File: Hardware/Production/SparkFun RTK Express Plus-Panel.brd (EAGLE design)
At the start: 219.3 x 141.9 mm, 507 parts, among them J13 Internal, J16 MICRO-SD-PUSH-PUSH-EXT-PIN, J17 Qwiic Right Angle, J19 External, J21 USB Female Type C Connector, J24 USB Female Type C Connector, J3 USB Female Type C Connector, J31 Qwiic Right Angle, J32 Internal, J38 MICRO-SD-PUSH-PUSH-EXT-PIN, J39 External, J4 External, J40 USB Female Type C Connector, J43 USB Female Type C Connector, J5 USB Female Type C Connector, J50 Qwiic Right Angle, J51 Internal, J57 MICRO-SD-PUSH-PUSH-EXT-PIN, Q1 SIL2308-TP, Q2 MBT3904DW1T1, Q3 MBT3904DW1T1, Q4 SIL2308-TP, Q5 MBT3904DW1T1, Q6 SIL2308-TP, U1 74HC4052D, U10 MCP73833, U11 U-BLOX_ZED_F9R, U12 CH340C, U13 LIS2DH12, U14 MAX17048, U15 STLQ015-3.3V, U16 MCP73833, U17 74HC4052D, U18 LIS2DH12, U19 ESP-WROOM-3232D-NARROW, U2 AP2112K-3.3, U20 NC7SZ14-D, U21 NC7SZ14-D, U22 U-BLOX_ZED_F9R, U23 AP2112K-3.3, U24 CH340C, U25 MAX17048, U26 STLQ015-3.3V, U27 MCP73833, U28 74HC4052D, U29 LIS2DH12, U3 AP2112K-3.3, U30 ESP-WROOM-3232D-NARROW, U31 NC7SZ14-D, U32 NC7SZ14-D, U33 U-BLOX_ZED_F9R, U4 STLQ015-3.3V, U5 ESP-WROOM-3232D-NARROW, U6 CH340C, U7 MAX17048, U8 NC7SZ14-D, U9 NC7SZ14-D

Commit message: Create panel files for v11 PCB
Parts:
- added R88, R92, R93: 10k, SparkFun-Resistors:0603
- added R89: 3.3k, SparkFun-Resistors:0603
- added R90, R91: 33, SparkFun-Resistors:1206_RA
- R10: value 10 -> 27
- R11: value 100k -> 27
- R12: value 5.1k -> 10
- R21, R70: value 5.1k -> 100k
- R32: value 1k -> 5.1k
- R35, R42: value 100k -> 5.1k
- R36: value 10k -> 1k
- R39, R55, R75, R84: value 10k -> 100k
- R40, R41: value 5.1k -> 10k
- R43: value 470 -> 5.1k
- R44: value 150k -> 100k
- R45: value 0 -> 470
- R46: value 10k -> 150k
- R47: value 1k -> 0
- R48, R57, R79, R87: value 33 -> 10k; device SparkFun-Resistors:1206_RA -> SparkFun-Resistors:0603
- R49: value 33 -> 1k; device SparkFun-Resistors:1206_RA -> SparkFun-Resistors:0603
- R51, R82: value 100k -> 33; device SparkFun-Resistors:0603 -> SparkFun-Resistors:1206_RA
- R52, R81: value 300k -> 33; device SparkFun-Resistors:0603 -> SparkFun-Resistors:1206_RA
- R54: value 10k -> 300k
- R56: value 3.3k -> 10k
- R58: value 33 -> 3.3k; device SparkFun-Resistors:1206_RA -> SparkFun-Resistors:0603
- R59, R60: value 27 -> 33; device SparkFun-Resistors:0603 -> SparkFun-Resistors:1206_RA
- R6, R8: value 27 -> 10k
- R61: value 10 -> 10k
- R62, R71: value 100k -> 10k
- R63, R64: value 5.1k -> 27
- R65: value 1k -> 10
- R67, R68: value 10k -> 5.1k
- R69: value 5.1k -> 1k
- R72: value 470 -> 10k
- R73: value 150k -> 5.1k
- R74: value 0 -> 5.1k
- R76: value 1k -> 470
- R77: value 33 -> 150k; device SparkFun-Resistors:1206_RA -> SparkFun-Resistors:0603
- R78: value 33 -> 0; device SparkFun-Resistors:1206_RA -> SparkFun-Resistors:0603
- R80: value 100k -> 1k
- R83: value 10k -> 33; device SparkFun-Resistors:0603 -> SparkFun-Resistors:1206_RA
- R85: value 3.3k -> 300k
- R86: value 33 -> 100k; device SparkFun-Resistors:1206_RA -> SparkFun-Resistors:0603
- U$1: device SparkFun-Aesthetics:QWIIC_4MM -> output:V110
- U$117, U$118, U$177, U$178: device output:V100 -> output:EXPRESS_PLUS0
- U$119, U$120, U$179, U$180: device output:EXPRESS_PLUS0 -> output:V110
- U$18: device SparkFun GPS RTK Surveyor:1553DBK-ENCLOSURE -> output:V110
- U$19: device output:LIPO0 -> output:#RTK#1
- U$2: device output:#RTK#1 -> SparkFun-Aesthetics:QWIIC_4MM
- U$20: device output:V100 -> SparkFun GPS RTK Surveyor:1553DBK-ENCLOSURE
- U$21: device output:V100 -> output:LIPO0
- moved U$1 113.7 mm to (34.2, 97.3), flipped to the top
- moved R73 102.3 mm to (186.6, 10.3), flipped to the top, turned to 180 degrees
- moved R74 98.0 mm to (179.6, 10.3), flipped to the top
- moved R69 97.9 mm to (151.3, 101.5), flipped to the bottom, turned to 90 degrees
- moved R32 94.4 mm to (106.9, 10.3), flipped to the top, turned to 180 degrees
- moved R43 91.2 mm to (110.9, 10.3), flipped to the top
- moved R65 87.2 mm to (170.4, 16.5), flipped to the top, turned to 0 degrees
- moved R79 86.5 mm to (148.6, 107.3), flipped to the bottom, turned to 0 degrees
- moved R41 86.4 mm to (80.9, 91.3), flipped to the bottom
- moved R35 86.3 mm to (98.9, 10.3), flipped to the top, turned to 0 degrees
- moved R70 85.1 mm to (182.6, 95.3), flipped to the bottom, turned to 270 degrees
- moved R40 83.6 mm to (80.9, 85.3), flipped to the bottom
- moved U$19 83.6 mm to (125.4, 26.8), flipped to the bottom
- moved R68 83.0 mm to (167.6, 10.3), flipped to the top
- moved U$20 81.6 mm to (102.9, 53.3), turned to 90 degrees
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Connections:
- removed net ESP_3V1: R56.2
- removed net ESP_3V2: R85.2
- removed net ESP_3V3: R34.2
- net 3.3V: now also R34.2, R6.2, R8.2
- net 3.3V1: now also R21.2, R39.2, R44.2, R58.2, R61.2, R62.2; no longer R11.2, R35.2, R42.2
- net 3.3V2: now also R70.2, R75.2, R89.2, R92.2, R93.2; no longer R62.2, R71.2
- net ANT_VCC1: now also R12.1; no longer R10.1
- net ANT_VCC2: now also R65.1; no longer R61.1
- net CC10: now also R67.2; no longer R63.2
- net CC11: now also R73.2; no longer R69.2
- net CC12: now also R74.2; no longer R70.2
- net CC5: now also R35.2; no longer R21.2
- net CC6: now also R32.2; no longer R12.2
- net CC7: now also R42.2; no longer R40.2
- net CC8: now also R43.2; no longer R41.2
- net CC9: now also R68.2; no longer R64.2
- net CHG_LED1: now also R45.2; no longer R43.2
- net CHG_LED2: now also R76.2; no longer R72.2
- net CHG_LED_RES1: now also R45.1; no longer R43.1
- net CHG_LED_RES2: now also R76.1; no longer R72.1
- net CHG_THERM2: now also R47.2, R48.2; no longer R44.2, R45.2
- net CHG_THERM3: now also R77.2, R78.2, R79.2; no longer R73.2, R74.2, R75.2
- net D+2: now also R10.1; no longer R6.1
- net D+4: now also R63.1; no longer R59.1
- net D-2: now also R11.1; no longer R8.1
- net D-4: now also R64.1; no longer R60.1
- net ESP32_!DTR1: now also R40.1; no longer R36.1
- net ESP32_!DTR2: now also R71.1; no longer R67.1
- net ESP32_!RTS1: now also R41.1; no longer R39.1
- net ESP32_!RTS2: now also R72.1; no longer R68.1
- net ESP32_EN1: now also R39.1; no longer R35.1
- net ESP32_EN2: now also R70.1; no longer R66.1
- net ESP_13/POWER_CTRL1: now also R53.1, R54.2; no longer R51.1, R52.2
- net ESP_13/POWER_CTRL2: now also R84.1, R85.2; no longer R80.1, R81.2
- net ESP_21/SDA1: now also R50.P7; no longer R48.P7
- net ESP_21/SDA2: now also R81.P7; no longer R77.P7
- net ESP_22/SCL1: now also R50.P8; no longer R48.P8
- net ESP_22/SCL2: now also R81.P8; no longer R77.P8
- net ESP_25/SD_!CS!1: now also R44.1; no longer R42.1
- net ESP_25/SD_!CS!2: now also R75.1; no longer R71.1
- net ESP_26/ZED_TX_READY_LV1: now also R51.P4; no longer R49.P4
- net ESP_26/ZED_TX_READY_LV2: now also R82.P4; no longer R78.P4
- net ESP_27/FAST_OFF1: now also R54.1; no longer R52.1
- net ESP_27/FAST_OFF2: now also R85.1; no longer R81.1
- net ESP_I16/ZED-TXO2: now also R50.P5; no longer R48.P5
- net ESP_I16/ZED-TXO3: now also R81.P5; no longer R77.P5
- net ESP_I34/ZED_TX_READY1: now also R51.P5; no longer R49.P5
- net ESP_I34/ZED_TX_READY2: now also R82.P5; no longer R78.P5
- net ESP_I35/DEVICE_SENSE1: now also R57.2, R58.1; no longer R55.2, R56.1
- net ESP_I35/DEVICE_SENSE2: now also R88.2, R89.1; no longer R84.2, R85.1
- net ESP_O17/ZED-RXI2: now also R49.2, R50.P6; no longer R47.2, R48.P6
- net ESP_O17/ZED-RXI3: now also R80.2, R81.P6; no longer R76.2, R77.P6
- net EXTINT_LV1: now also R52.P2; no longer R50.P2
- net EXTINT_LV2: now also R83.P2; no longer R79.P2
- net EXT_DIR: now also R6.1
- net EXT_DIR1: now also R61.1
- net EXT_DIR2: now also R92.1
- net EXT_WT: now also R8.1
- net EXT_WT1: now also R62.1
- net EXT_WT2: now also R93.1
- net FENCE_LV1: now also R59.P6; no longer R57.P6
- net FENCE_LV2: now also R90.P6; no longer R86.P6
- net GND1: now also R35.1, R36.1, R42.1, R43.1, R48.1, R57.1; no longer R11.1, R12.1, R40.1, R41.1, R44.1, R55.1
- net GND2: now also R66.1, R67.1, R68.1, R74.1, R77.1, R79.1, R88.1; no longer R62.1, R63.1, R64.1, R65.1, R70.1, R75.1, R84.1
- net N$1: now also R10.2; no longer R6.2
- net N$10: now also R41.2; no longer R39.2
- net N$17: now also R47.1; no longer R45.1
- net N$18: now also R49.1; no longer R47.1
- net N$19: now also R55.1; no longer R53.1
- net N$20: now also R60.P4; no longer R58.P4
- net N$21: now also R60.P3; no longer R58.P3
- net N$22: now also R63.2; no longer R59.2
- net N$23: now also R64.2; no longer R60.2
- net N$26: now also R65.2; no longer R61.2
- net N$27: now also R71.2; no longer R67.2
- net N$28: now also R72.2; no longer R68.2
- net N$31: now also R78.1; no longer R74.1
- net N$33: now also R80.1; no longer R76.1
- net N$34: now also R86.1; no longer R82.1
- net N$35: now also R91.P4; no longer R87.P4
- net N$36: now also R91.P3; no longer R87.P3
- net N$7: now also R11.2; no longer R8.2
- net N$8: now also R12.2; no longer R10.2
- net N$9: now also R40.2; no longer R36.2
- net POWER_BTN1: now also R56.1; no longer R54.1
- net POWER_BTN2: now also R87.1; no longer R83.1
- net PPS_LV1: now also R52.P1; no longer R50.P1
- net PPS_LV2: now also R83.P1; no longer R79.P1
- net PROG2: now also R36.2; no longer R32.2
- net PROG3: now also R69.2; no longer R65.2
- net RTK_STAT_LV1: now also R59.P5; no longer R57.P5
- net RTK_STAT_LV2: now also R90.P5; no longer R86.P5
- net RX2_LV1: now also R60.P2; no longer R58.P2
- net RX2_LV2: now also R91.P2; no longer R87.P2
- net RXLV1: now also R50.P3; no longer R48.P3
- net RXLV2: now also R81.P3; no longer R77.P3
- net SCL_LV1: now also R50.P1; no longer R48.P1
- net SCL_LV2: now also R81.P1; no longer R77.P1
- net SDA_LV1: now also R50.P2; no longer R48.P2
- net SDA_LV2: now also R81.P2; no longer R77.P2
- net TX2_LV1: now also R60.P1; no longer R58.P1
- net TX2_LV2: now also R91.P1; no longer R87.P1
- net TXLV1: now also R50.P4; no longer R48.P4
- net TXLV2: now also R81.P4; no longer R77.P4
- net VOUT1: now also R53.2; no longer R51.2
- net VOUT2: now also R84.2; no longer R80.2
- net V_RAW1: now also R55.2, R56.2; no longer R53.2, R54.2
- net V_RAW2: now also R86.2, R87.2; no longer R82.2, R83.2
- net ZED-RXI1: now also R60.P7; no longer R58.P7
- net ZED-RXI3: now also R91.P7; no longer R87.P7
- net ZED-TXO1: now also R60.P8; no longer R58.P8
- net ZED-TXO3: now also R91.P8; no longer R87.P8
- net ZED_!RESET!1: now also R51.P7; no longer R49.P7
- net ZED_!RESET!2: now also R82.P7; no longer R78.P7
- net ZED_!RESET!_LV1: now also R51.P2; no longer R49.P2
- net ZED_!RESET!_LV2: now also R82.P2; no longer R78.P2
- net ZED_!SAFE!1: now also R51.P8; no longer R49.P8
- net ZED_!SAFE!2: now also R82.P8; no longer R78.P8
- net ZED_!SAFE!_LV1: now also R51.P1; no longer R49.P1
- net ZED_!SAFE!_LV2: now also R82.P1; no longer R78.P1
- net ZED_DIR1: now also R60.P6; no longer R58.P6
- net ZED_DIR2: now also R91.P6; no longer R87.P6
- net ZED_D_SEL1: now also R51.P6; no longer R49.P6
- net ZED_D_SEL2: now also R82.P6; no longer R78.P6
- net ZED_D_SEL_LV1: now also R51.P3; no longer R49.P3
- net ZED_D_SEL_LV2: now also R82.P3; no longer R78.P3
- net ZED_EXTINT1: now also R52.P7; no longer R50.P7
- net ZED_EXTINT2: now also R83.P7; no longer R79.P7
- net ZED_FENCE_STAT1: now also R59.P3; no longer R57.P3
- net ZED_FENCE_STAT2: now also R90.P3; no longer R86.P3
- net ZED_PPS_STAT1: now also R52.P8; no longer R50.P8
- net ZED_PPS_STAT2: now also R83.P8; no longer R79.P8
- net ZED_RTK_STAT1: now also R59.P4; no longer R57.P4
- net ZED_RTK_STAT2: now also R90.P4; no longer R86.P4
- net ZED_WT1: now also R60.P5; no longer R58.P5
- net ZED_WT2: now also R91.P5; no longer R87.P5
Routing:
- net 3.3V1: track 326.7 -> 340.8 mm, vias 11 -> 12
- net 3.3V2: track 326.7 -> 340.8 mm, vias 11 -> 12
- net 3.3V: track 326.7 -> 340.8 mm, vias 11 -> 12
- net EXT_WT: track 53.8 -> 54.9 mm
- net EXT_WT2: track 53.8 -> 54.9 mm
- net EXT_WT1: track 53.8 -> 54.9 mm
- net EXT_DIR1: track 62.0 -> 63.1 mm
- net EXT_DIR: track 62.0 -> 63.1 mm
- net EXT_DIR2: track 62.0 -> 63.1 mm

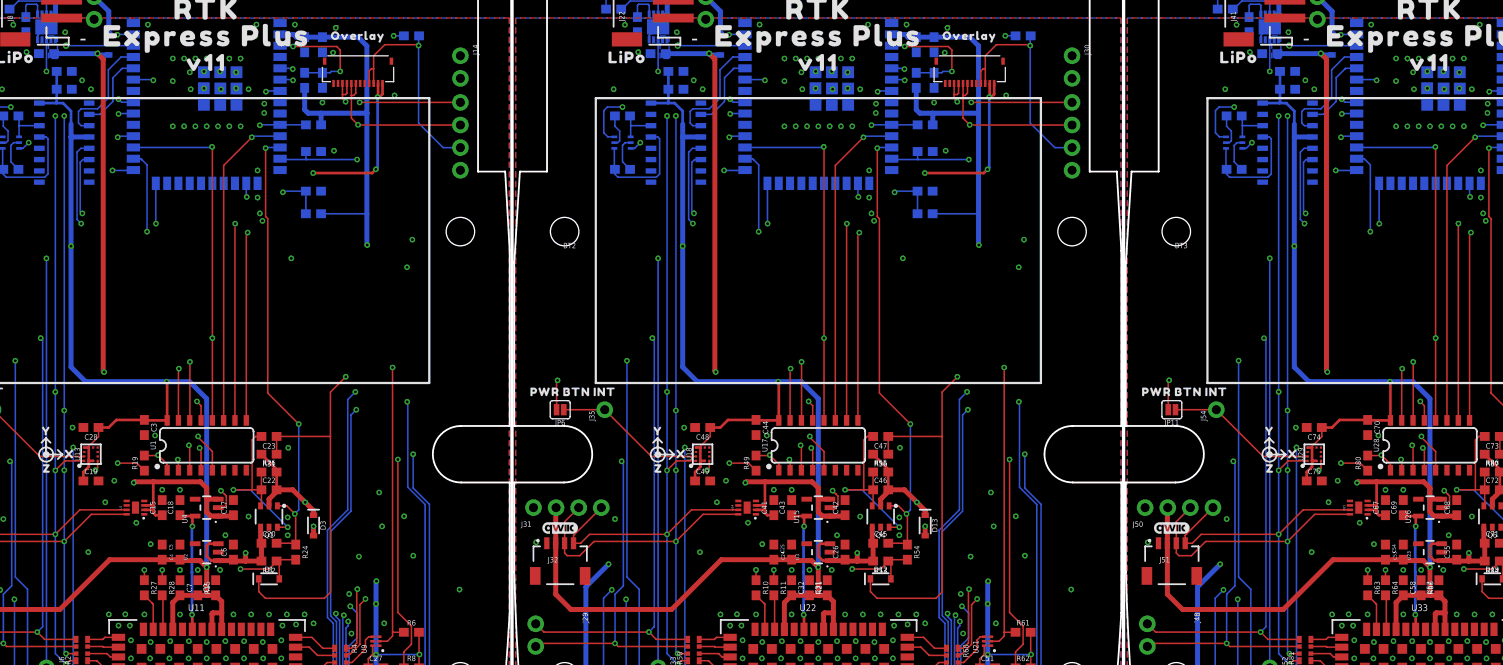
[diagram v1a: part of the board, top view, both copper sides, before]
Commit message: v12 PCB - remove ground plane from accelerometer. Remove old files.
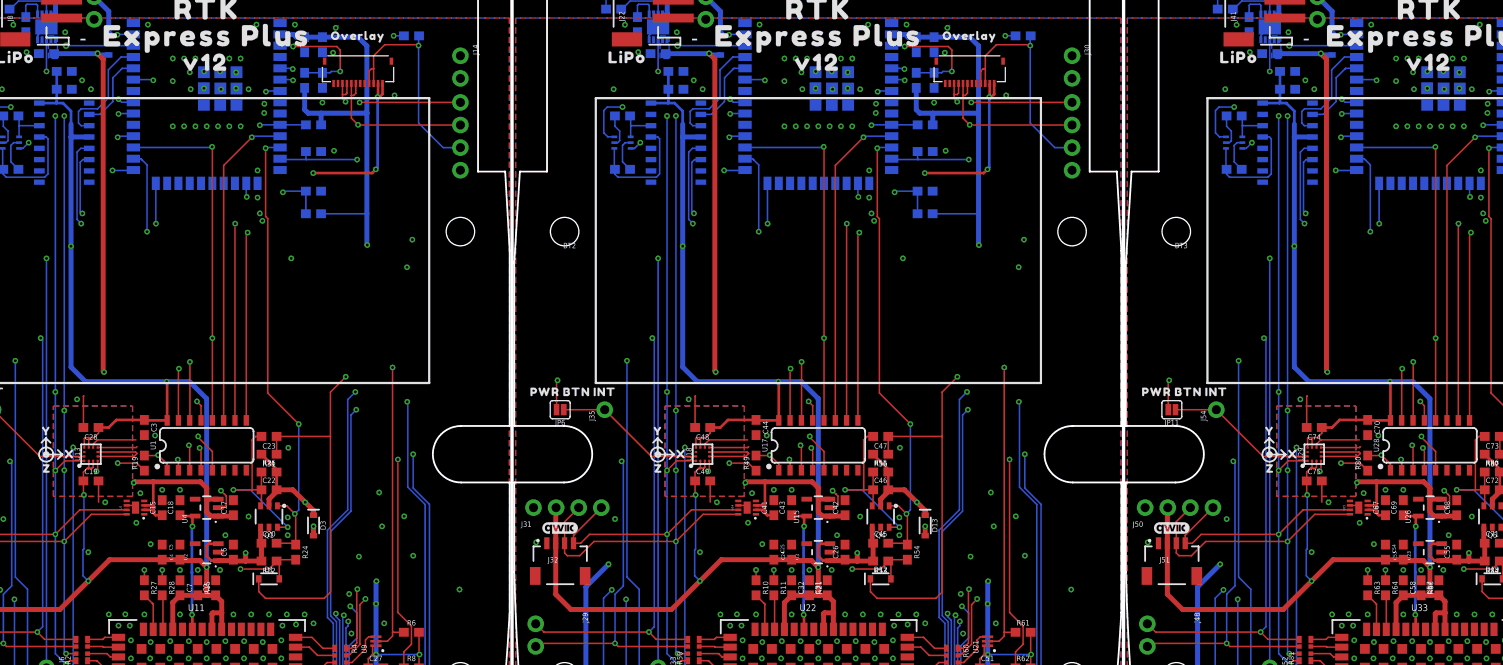
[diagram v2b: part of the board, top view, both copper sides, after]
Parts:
- removed U$178: (no value), output:EXPRESS_PLUS0
- removed U$179, U$180: (no value), output:V110
- U$1, U$119: device output:V110 -> SparkFun-Aesthetics:QWIIC_4MM
- U$100: device output:#SDA#0 -> output:#D_SEL#0
- U$101: device output:#D_SEL#0 -> SparkFun-Aesthetics:QWIIC_4MM
- U$102: device SparkFun-Aesthetics:QWIIC_4MM -> output:#TX_RDY#0
- U$103: device output:#TX_RDY#0 -> output:CHG2
- U$104: device output:CHG2 -> output:GND3
- U$105: device output:GND3 -> output:PWR0
- U$106: device output:PWR0 -> output:SETUP1
- U$107: device output:SETUP1 -> output:X0
- U$108: device output:X0 -> output:Y1
- U$109: device output:Y1 -> output:Z2
- U$110: device output:Z2 -> output:INT0
- U$111: device output:INT0 -> output:PWR_BTN1
- U$112: device output:PWR_BTN1 -> output:OVERLAY0
- U$113: device output:OVERLAY0 -> output:L1#L20
- U$114: device output:L1#L20 -> output:ACTIVE1
- U$115: device output:ACTIVE1 -> output:ANTENNA2
- U$116, U$176: device output:ANTENNA2 -> output:EXPRESS_PLUS0
- U$118, U$177: device output:EXPRESS_PLUS0 -> output:V120
- U$120: device output:V110 -> output:#RTK#1
- U$121: device SparkFun-Aesthetics:QWIIC_4MM -> SparkFun GPS RTK Surveyor:1553DBK-ENCLOSURE
- U$122: device output:#RTK#1 -> output:LIPO0
- U$123: device SparkFun GPS RTK Surveyor:1553DBK-ENCLOSURE -> output:U#BLOX0
- U$124: device output:LIPO0 -> output:USB1
- U$125: device output:U#BLOX0 -> output:SERIAL20
- U$126: device output:USB1 -> output:SERIAL10
- U$127: device output:SERIAL20 -> output:#RX2#2
- U$128: device output:SERIAL10 -> output:#TX2#1
- U$129: device output:#RX2#2 -> output:#RX1#2
- U$130: device output:#TX2#1 -> output:#TX1#1
- U$131: device output:#RX1#2 -> output:#3V3#0
- U$132, U$149: device output:#TX1#1 -> output:#GND#0
- U$133, U$57: device output:#3V3#0 -> output:#GND#0
- U$134, U$59: device output:#GND#0 -> output:NMEA1
- U$135: device output:#GND#0 -> output:RADIO0
- U$136: device output:NMEA1 -> output:##RST##4
- U$137: device output:RADIO0 -> output:##SAFE##5
- U$138: device output:##RST##4 -> output:#FENCE#3
- U$139: device output:##SAFE##5 -> output:#3#5#5V#0
- U$140: device output:#FENCE#3 -> output:#PPS#0
- U$141: device output:#3#5#5V#0 -> output:#RX#2
- U$142: device output:#PPS#0 -> output:ZED0
- U$143: device output:#RX#2 -> output:#TX#1
- U$144: device output:ZED0 -> output:USB1
- U$145: device output:#TX#1 -> output:ESP320
- U$146: device output:USB1 -> output:#3V3#0
- U$147: device output:ESP320 -> output:#TX1#1
- U$148: device output:#3V3#0 -> output:#RX1#2
- U$150: device output:#RX1#2 -> output:MICROSD0
- U$151: device output:#GND#0 -> output:#GND#1
- U$152: device output:MICROSD0 -> output:#ESP_RST#0
- U$153: device output:#GND#1 -> output:RTK0
- U$154, U$94: device output:#ESP_RST#0 -> output:RTK0
- U$155, U$96: device output:RTK0 -> output:#GND#2
- U$156: device output:RTK0 -> output:#3V3#2
- U$157: device output:#GND#2 -> output:#SCL#1
- U$158: device output:#3V3#2 -> output:#SDA#0
- U$159: device output:#SCL#1 -> output:#D_SEL#0
- U$160: device output:#SDA#0 -> SparkFun-Aesthetics:QWIIC_4MM
- U$161: device output:#D_SEL#0 -> output:#TX_RDY#0
- U$162: device SparkFun-Aesthetics:QWIIC_4MM -> output:CHG2
- U$163: device output:#TX_RDY#0 -> output:GND3
- U$164: device output:CHG2 -> output:PWR0
- U$165: device output:GND3 -> output:SETUP1
- U$166: device output:PWR0 -> output:X0
- U$167: device output:SETUP1 -> output:Y1
- U$168: device output:X0 -> output:Z2
- U$169: device output:Y1 -> output:INT0
- U$170: device output:Z2 -> output:PWR_BTN1
- U$171: device output:INT0 -> output:OVERLAY0
- U$172: device output:PWR_BTN1 -> output:L1#L20
- U$173: device output:OVERLAY0 -> output:ACTIVE1
- U$174: device output:L1#L20 -> output:ANTENNA2
- U$175: device output:ACTIVE1 -> output:EXPRESS_PLUS0
- U$18: device output:V110 -> SparkFun GPS RTK Surveyor:1553DBK-ENCLOSURE
- U$19: device output:#RTK#1 -> output:V120
- U$2: device SparkFun-Aesthetics:QWIIC_4MM -> output:#RTK#1
- U$20: device SparkFun GPS RTK Surveyor:1553DBK-ENCLOSURE -> output:LIPO0
- U$21: device output:LIPO0 -> output:U#BLOX0
- U$25: device output:U#BLOX0 -> output:USB1
- U$31: device output:USB1 -> output:SERIAL20
- U$37: device output:SERIAL20 -> output:SERIAL10
- U$44: device output:SERIAL10 -> output:#RX2#2
- U$51: device output:#RX2#2 -> output:#TX2#1
- U$52: device output:#TX2#1 -> output:#RX1#2
- U$53: device output:#RX1#2 -> output:#TX1#1
- U$54: device output:#TX1#1 -> output:#3V3#0
- U$61: device output:NMEA1 -> output:RADIO0
- U$62: device output:RADIO0 -> output:##RST##4
- U$63: device output:##RST##4 -> output:##SAFE##5
- U$64: device output:##SAFE##5 -> output:#FENCE#3
- U$69: device output:#FENCE#3 -> output:#3#5#5V#0
- U$71: device output:#3#5#5V#0 -> output:#PPS#0
- U$73: device output:#PPS#0 -> output:#RX#2
- U$75: device output:#RX#2 -> output:ZED0
- U$76: device output:ZED0 -> output:#TX#1
- U$77: device output:#TX#1 -> output:USB1
- U$78: device output:USB1 -> output:ESP320
- U$79: device output:ESP320 -> output:#3V3#0
- U$80: device output:#3V3#0 -> output:#TX1#1
- U$81: device output:#TX1#1 -> output:#RX1#2
- U$89: device output:#RX1#2 -> output:#GND#0
- U$90: device output:#GND#0 -> output:MICROSD0
- U$91: device output:MICROSD0 -> output:#GND#1
- U$92: device output:#GND#1 -> output:#ESP_RST#0
- U$97: device output:#GND#2 -> output:#3V3#2
- U$98: device output:#3V3#2 -> output:#SCL#1
- U$99: device output:#SCL#1 -> output:#SDA#0
- moved U$19 115.4 mm to (34.1, 97.3), flipped to the top
- moved U$1 113.7 mm to (102.9, 6.65), flipped to the bottom
- moved U$119 113.7 mm to (171.6, 6.65), flipped to the bottom
- moved U$120 93.5 mm to (194.1, 26.8)
- moved U$124 92.9 mm to (169.5, 7.03)
- moved U$21 91.3 mm to (99.9, 8.43)
- moved U$173 91.1 mm to (160.0, 13.8)
- moved U$113 89.7 mm to (91.3, 15.3)
- moved U$176 88.8 mm to (171.6, 100.3)
- moved U$152 85.8 mm to (199.5, 98.0), turned to 0 degrees
- moved U$122 83.6 mm to (150.1, 97.9), flipped to the top
- moved U$91 83.2 mm to (130.8, 95.4), turned to 0 degrees
- moved U$151 77.6 mm to (199.5, 95.4), flipped to the bottom, turned to 0 degrees
- moved U$103 75.8 mm to (128.7, 87.8)
- moved U$163 73.9 mm to (197.5, 85.2)
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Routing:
- net GND2: track 18.1 -> 44.0 mm
- net GND1: track 18.1 -> 44.0 mm
- net GND: track 18.1 -> 44.0 mm
- net 3.3V2: track 340.8 -> 353.1 mm, vias 12 -> 14
- net 3.3V: track 340.8 -> 353.1 mm, vias 12 -> 14
- net 3.3V1: track 340.8 -> 353.1 mm, vias 12 -> 14
